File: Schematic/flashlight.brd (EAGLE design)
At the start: 33.2 x 17.8 mm, 2 parts, among them IC1 AMC7135SOT-89

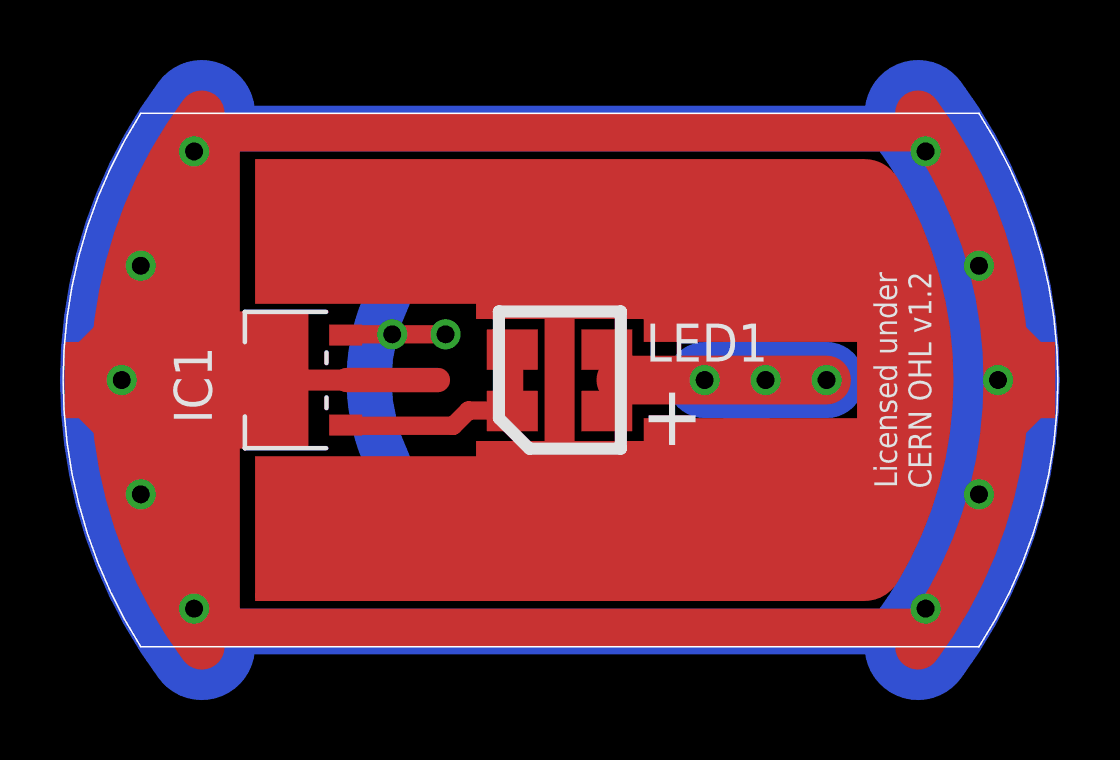
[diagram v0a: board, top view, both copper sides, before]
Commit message: fix pin layout of AMC7135 package
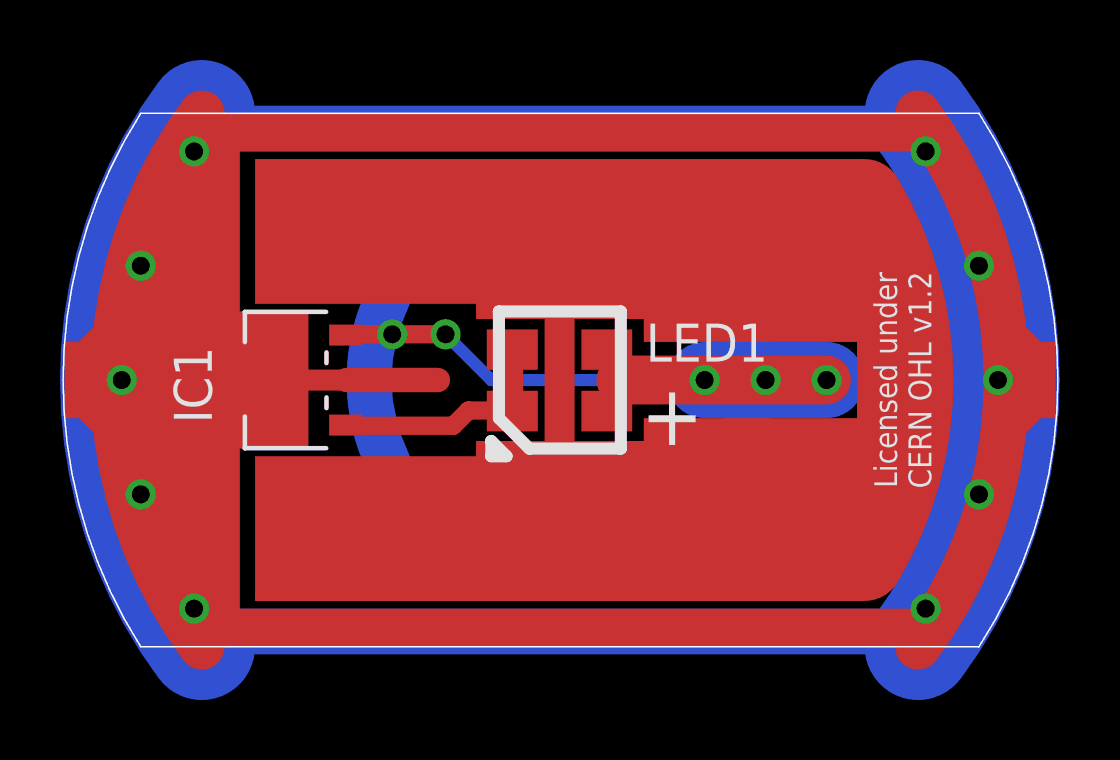
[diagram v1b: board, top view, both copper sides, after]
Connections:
- net N$28: now also IC1.1; no longer IC1.2
- net N$3: now also IC1.2; no longer IC1.1
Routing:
- net N$29: track 3.30 -> 23.5 mm, vias 2 -> 4
- net N$14: track 10.9 -> 0.00 mm, vias 2 -> 0
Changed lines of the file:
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@@
 <text x="27.94" y="8.89" size="0.762" layer="25" rot="R90" align="center">Licensed under
 CERN OHL v1.2</text>
+<wire x1="14.224" y1="6.35" x2="14.732" y2="6.35" width="0.4064" layer="25"/>
+<wire x1="14.732" y1="6.35" x2="14.224" y2="6.858" width="0.4064" layer="25"/>
+<wire x1="14.224" y1="6.858" x2="14.224" y2="6.35" width="0.4064" layer="25"/>
 </plain>
 <attributes>
@@
 <via x="23.368" y="8.89" extent="1-16" drill="0.6"/>
 </signal>
-<signal name="N$14">
-<via x="21.336" y="8.89" extent="1-16" drill="0.6"/>
-<via x="25.4" y="8.89" extent="1-16" drill="0.6"/>
-<wire x1="25.4" y1="8.89" x2="18.542" y2="8.89" width="1.6256" layer="1"/>
-<wire x1="25.4" y1="8.89" x2="21.336" y2="8.89" width="2.54" layer="16"/>
-</signal>
 <signal name="N$15">
 <wire x1="2.032" y1="6.858" x2="2.032" y2="7.366" width="0.4064" layer="1"/>
@@
 <wire x1="28.448" y1="0" x2="28.448" y2="0" width="0" layer="19" extent="1-16"/>
 <wire x1="4.572" y1="17.78" x2="28.448" y2="17.78" width="0" layer="19" extent="1-1"/>
-<wire x1="-0.508" y1="17.78" x2="4.572" y2="17.78" width="0" layer="19" extent="1-16"/>
-<wire x1="4.572" y1="17.78" x2="-0.508" y2="17.78" width="0" layer="19" extent="16-16"/>
-<wire x1="-10.668" y1="25.4" x2="4.572" y2="17.78" width="0" layer="19" extent="16-16"/>
+<wire x1="4.572" y1="17.78" x2="4.572" y2="17.78" width="0" layer="19" extent="1-16"/>
 </signal>
 <signal name="N$2">
@@
 <signal name="N$3">
 <contactref element="LED1" pad="C@1"/>
-<contactref element="IC1" pad="1"/>
-<wire x1="9.37" y1="10.39" x2="14.925" y2="7.855" width="0" layer="19" extent="1-1"/>
+<contactref element="IC1" pad="2"/>
+<wire x1="9.37" y1="7.39" x2="14.925" y2="7.855" width="0" layer="19" extent="1-1"/>
 </signal>
 <signal name="N$28">
 <contactref element="LED1" pad="A@1"/>
-<contactref element="IC1" pad="2"/>
-<wire x1="9.37" y1="7.39" x2="18.075" y2="7.855" width="0" layer="19" extent="1-1"/>
+<contactref element="IC1" pad="1"/>
+<wire x1="9.37" y1="10.39" x2="18.075" y2="7.855" width="0" layer="19" extent="1-1"/>
 </signal>
 <signal name="N$12">
@@
 <via x="10.922" y="10.414" extent="1-16" drill="0.6"/>
 <via x="12.7" y="10.414" extent="1-16" drill="0.6"/>
+<via x="21.336" y="8.89" extent="1-16" drill="0.6"/>
+<via x="25.4" y="8.89" extent="1-16" drill="0.6"/>
+<wire x1="25.4" y1="8.89" x2="18.542" y2="8.89" width="1.6256" layer="1"/>
+<wire x1="25.4" y1="8.89" x2="21.336" y2="8.89" width="2.54" layer="16"/>
+<wire x1="12.7" y1="10.414" x2="14.224" y2="8.89" width="0.4064" layer="16"/>
+<wire x1="14.224" y1="8.89" x2="21.336" y2="8.89" width="0.4064" layer="16"/>
 </signal>
 <signal name="N$30">

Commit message: cleanup routing on the board
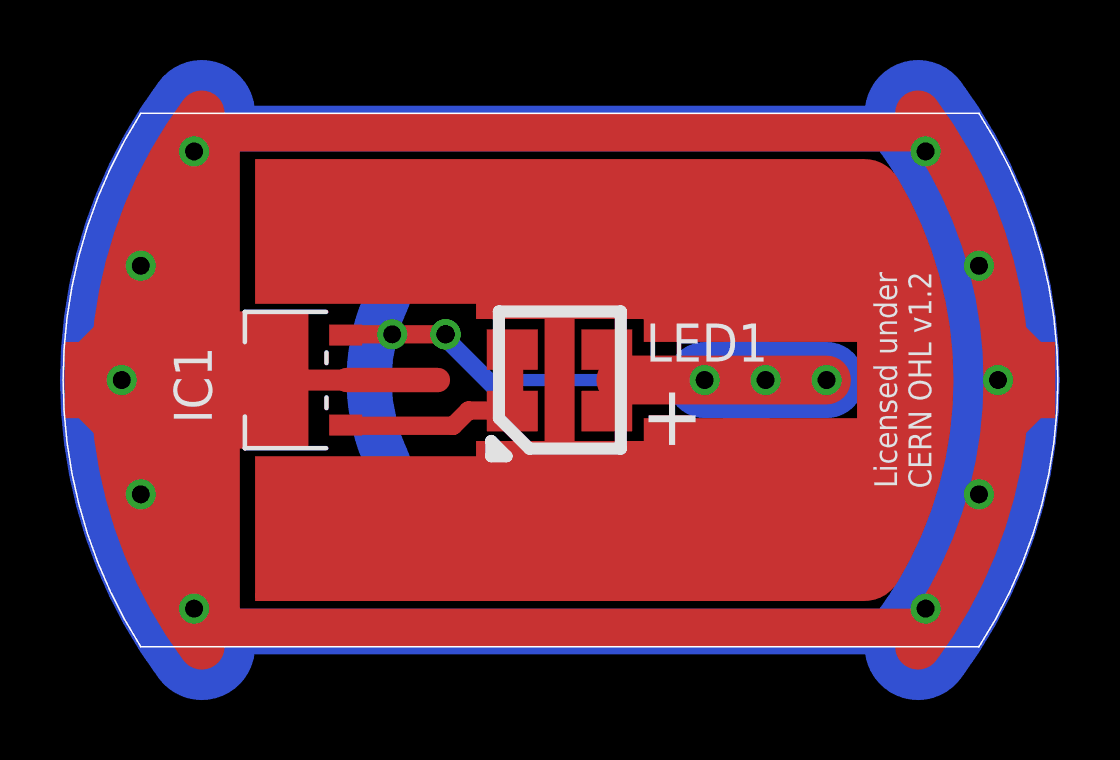
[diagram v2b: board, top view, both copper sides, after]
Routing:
- net N$5: track 71.1 -> 17.8 mm
- net N$24: track 0.00 -> 17.8 mm
- net N$23: track 0.00 -> 17.8 mm
- net N$14: track 0.00 -> 17.8 mm
- net N$28: track 0.00 -> 6.83 mm, vias 0 -> 1
- net N$3: track 0.00 -> 5.76 mm
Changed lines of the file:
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@@
 <wire x1="32.512" y1="7.874" x2="31.75" y2="7.112" width="0.4064" layer="1"/>
+</signal>
+<signal name="N$23">
+<wire x1="4.572" y1="17.78" x2="4.572" y2="0" width="3.556" layer="16" curve="73.34" cap="flat"/>
+</signal>
+<signal name="N$14">
+<wire x1="4.572" y1="17.78" x2="4.572" y2="0" width="1.524" layer="1" curve="73.34" cap="flat"/>
+</signal>
+<signal name="N$24">
+<wire x1="28.448" y1="0" x2="28.448" y2="17.78" width="3.556" layer="16" curve="73.34" cap="flat"/>
 </signal>
 <signal name="N$5">
 <wire x1="28.448" y1="17.78" x2="28.448" y2="0" width="1.524" layer="1" curve="-73.34" cap="flat"/>
-<wire x1="4.572" y1="17.78" x2="4.572" y2="0" width="1.524" layer="1" curve="73.34" cap="flat"/>
-<wire x1="28.448" y1="0" x2="28.448" y2="17.78" width="3.556" layer="16" curve="73.34" cap="flat"/>
-<wire x1="4.572" y1="17.78" x2="4.572" y2="0" width="3.556" layer="16" curve="73.34" cap="flat"/>
-<wire x1="28.448" y1="0" x2="28.448" y2="0" width="0" layer="19" extent="1-16"/>
-<wire x1="4.572" y1="17.78" x2="28.448" y2="17.78" width="0" layer="19" extent="1-1"/>
-<wire x1="4.572" y1="17.78" x2="4.572" y2="17.78" width="0" layer="19" extent="1-16"/>
 </signal>
 <signal name="N$2">
@@
 <contactref element="LED1" pad="C@1"/>
 <contactref element="IC1" pad="2"/>
-<wire x1="9.37" y1="7.39" x2="14.925" y2="7.855" width="0" layer="19" extent="1-1"/>
+<wire x1="9.37" y1="7.39" x2="12.978" y2="7.39" width="0.4064" layer="1"/>
+<wire x1="12.978" y1="7.39" x2="13.462" y2="7.874" width="0.4064" layer="1"/>
+<wire x1="13.462" y1="7.874" x2="14.906" y2="7.874" width="0.4064" layer="1"/>
+<wire x1="14.906" y1="7.874" x2="14.925" y2="7.855" width="0.4064" layer="1"/>
 </signal>
 <signal name="N$28">
 <contactref element="LED1" pad="A@1"/>
 <contactref element="IC1" pad="1"/>
-<wire x1="9.37" y1="10.39" x2="18.075" y2="7.855" width="0" layer="19" extent="1-1"/>
+<wire x1="9.37" y1="10.39" x2="12.676" y2="10.39" width="0.4064" layer="1"/>
+<wire x1="12.676" y1="10.39" x2="12.7" y2="10.414" width="0.4064" layer="1"/>
+<via x="12.7" y="10.414" extent="1-16" drill="0.6"/>
+<wire x1="12.7" y1="10.414" x2="12.7" y2="10.16" width="0.4064" layer="16"/>
+<wire x1="12.7" y1="10.16" x2="14.986" y2="7.874" width="0.4064" layer="16"/>
+<wire x1="14.986" y1="7.874" x2="18.075" y2="7.855" width="0" layer="19" extent="1-16"/>
 </signal>
 <signal name="N$12">
